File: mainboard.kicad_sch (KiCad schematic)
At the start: 90 parts, among them J1 Conn 02x05 1.27mm, J10 Conn -Z 02x05 2.00 mm, J11 Conn +X 02x05 2.00 mm, J12 Conn -X 02x05 2.00 mm, J2 USB_C_Receptacle_USB2.0, J3 Conn 02x10 1.27mm, J4 Conn +Z 02x05 2.00 mm, J5 Conn -Z 02x05 2.00 mm, J6 Conn +X 02x05 2.00 mm, J7 Conn -X 02x05 2.00 mm, J8 U.FL-R-SMT-1, J9 Conn +Z 02x05 2.00 mm, Q1 DMG2301L, SW1 KMR231NG, U1 ATSAMD51J20A-M, U10 USBLC6-2SC6, U2 MAX706RESA+, U3 AP2112K-3.3, U4 MR25H40, U5 BMX160, U6 RFM98PW, U7 DRV8830DRC, U8 DRV8830DRC, U9 DRV8830DRC, Y1 32.768kHz

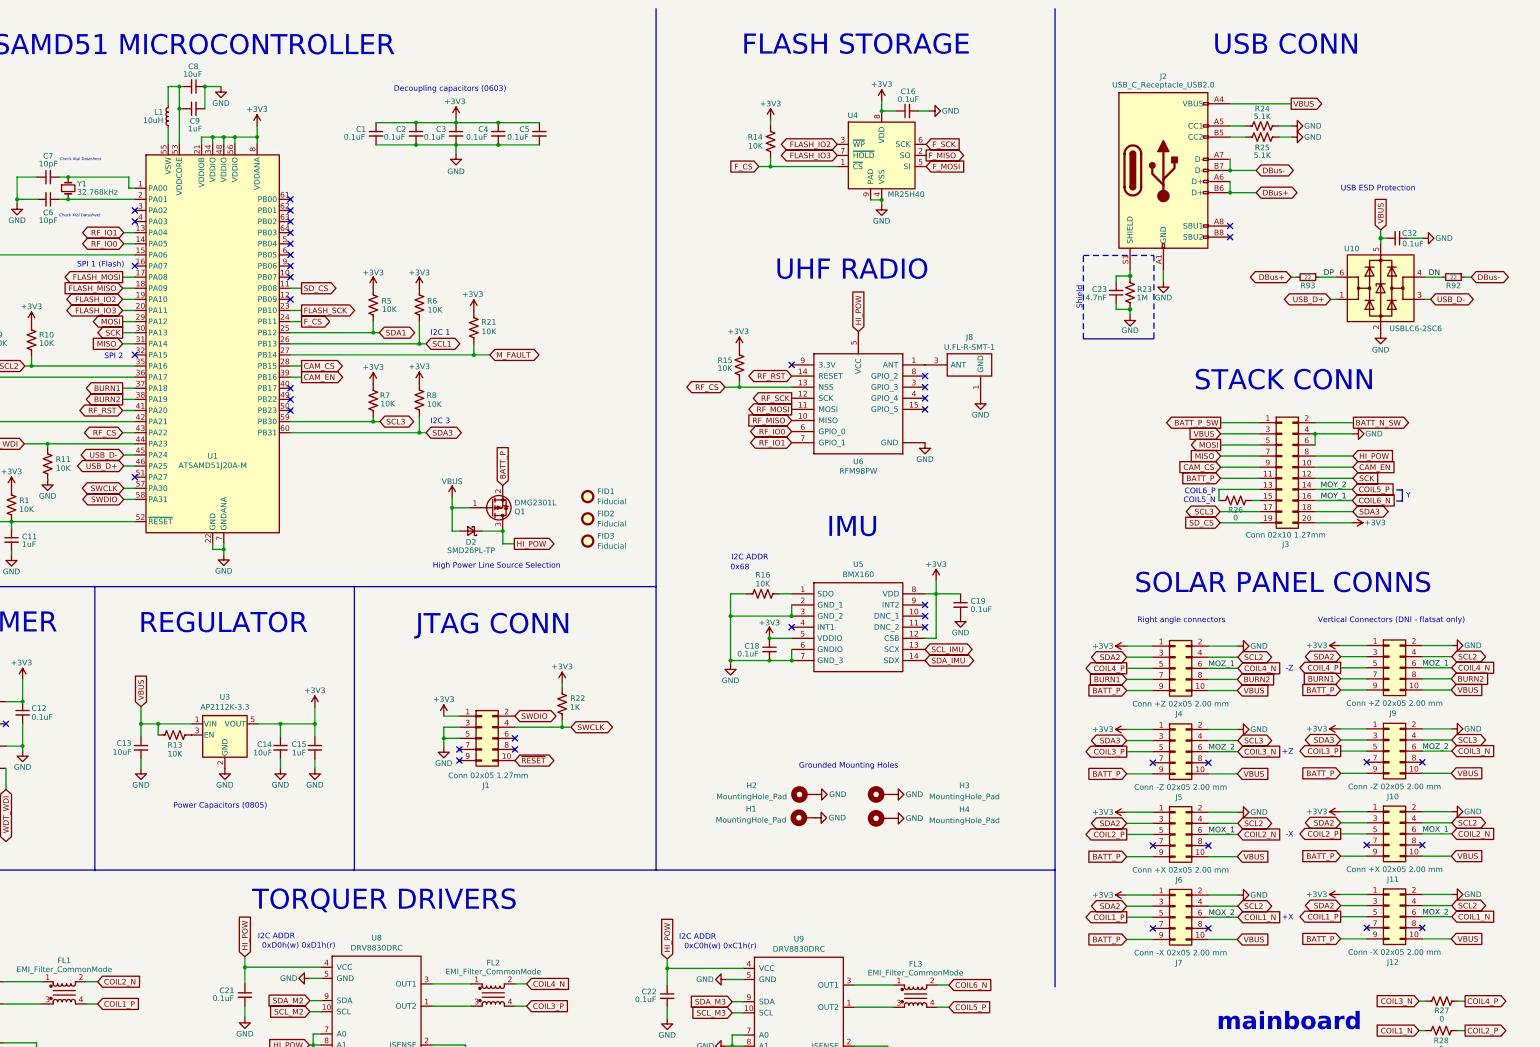
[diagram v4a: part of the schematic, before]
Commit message: Updated stack connectors and added SPDT switch
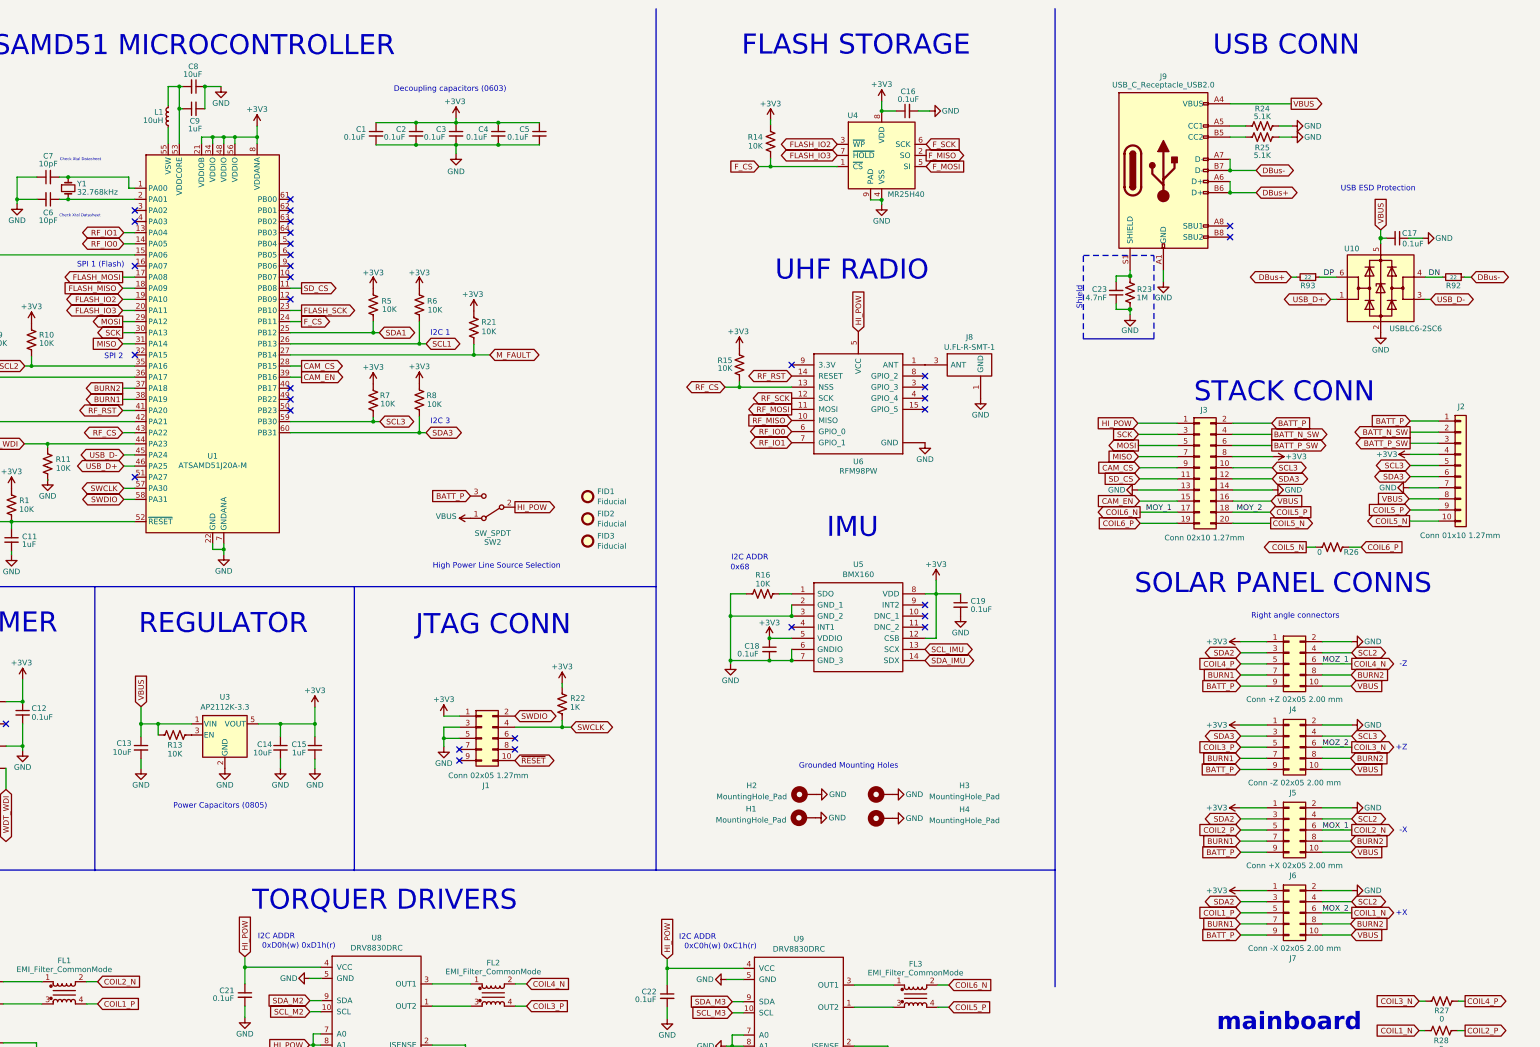
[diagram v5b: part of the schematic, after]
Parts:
- removed D2: SMD26PL-TP, Diode_SMD:D_SOD-123F, symbol Device:D_Schottky_Small
- removed J10: Conn -Z 02x05 2.00 mm, Connector_PinSocket_1.27mm:PinSocket_2x05_P1.27mm_Vertical_SMD, symbol Connector_Generic:Conn_02x05_Odd_Even
- removed J11: Conn +X 02x05 2.00 mm, Connector_PinSocket_1.27mm:PinSocket_2x05_P1.27mm_Vertical_SMD, symbol Connector_Generic:Conn_02x05_Odd_Even
- removed J12: Conn -X 02x05 2.00 mm, Connector_PinSocket_1.27mm:PinSocket_2x05_P1.27mm_Vertical_SMD, symbol Connector_Generic:Conn_02x05_Odd_Even
- removed J9: Conn +Z 02x05 2.00 mm, Connector_PinSocket_1.27mm:PinSocket_2x05_P1.27mm_Vertical_SMD, symbol Connector_Generic:Conn_02x05_Odd_Even
- removed Q1: DMG2301L, Package_TO_SOT_SMD:SOT-23, symbol Transistor_FET:DMG2301L
- added J2: Conn 01x10 1.27mm, Connector_PinSocket_1.27mm:PinSocket_1x10_P1.27mm_Vertical, symbol Connector_Generic:Conn_01x10
- added SW2: SW_SPDT, mainboard:SW_PCM12SMTR, symbol Switch:SW_SPDT
- J3: footprint Connector_PinHeader_1.27mm:PinHeader_2x10_P1.27mm_Vertical -> Connector_PinSocket_1.27mm:PinSocket_2x10_P1.27mm_Vertical
- renumbered C32 to C17, J2 to J9
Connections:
- net +3V3: now also J3.8 (Pin_8), J2.4 (Pin_4); no longer J3.20 (Pin_20)
- net BATT_N_SW: now also J3.4 (Pin_4), J2.2 (Pin_2); no longer J3.2 (Pin_2)
- net BATT_P: now also J3.2 (Pin_2), J2.1 (Pin_1), SW2.3 (C); no longer J3.11 (Pin_11)
- net BATT_P_SW: now also J3.6 (Pin_6), J2.3 (Pin_3); no longer J3.1 (Pin_1)
- net BURN1: now also J5.7 (Pin_7), J6.7 (Pin_7), J7.7 (Pin_7), U1.38 (PA19); no longer U1.37 (PA18)
- net BURN2: now also J5.8 (Pin_8), J6.8 (Pin_8), J7.8 (Pin_8), U1.37 (PA18); no longer U1.38 (PA19)
- net CAM_EN: now also J3.15 (Pin_15); no longer J3.10 (Pin_10)
- net COIL5_P: now also J3.18 (Pin_18), J2.9 (Pin_9); no longer J3.14 (Pin_14)
- net COIL6_N: now also J3.17 (Pin_17); no longer J3.16 (Pin_16)
- net GND: now also J3.13 (Pin_13), J3.14 (Pin_14), J2.7 (Pin_7); no longer J3.4 (Pin_4), J3.6 (Pin_6)
- net HI_POW: now also J3.1 (Pin_1), SW2.2 (B); no longer J3.8 (Pin_8)
- net SCK: now also J3.3 (Pin_3); no longer J3.12 (Pin_12)
- net SCL3: now also J3.10 (Pin_10), J2.5 (Pin_5); no longer J3.17 (Pin_17)
- net SDA3: now also J3.12 (Pin_12), J2.6 (Pin_6); no longer J3.18 (Pin_18)
- net SD_CS: now also J3.11 (Pin_11); no longer J3.19 (Pin_19)
- net VBUS: now also J3.16 (Pin_16), J2.8 (Pin_8), SW2.1 (A); no longer J3.3 (Pin_3)
- net COIL6_P: now reaches R26.1
- net COIL6_P: now also J3.19 (Pin_19); no longer J3.13 (Pin_13)
- net COIL5_N: now reaches R26.2
- net COIL5_N: now also J3.20 (Pin_20), J2.10 (Pin_10); no longer J3.15 (Pin_15)
- no-connect marks 47 -> 35
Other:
- note removed: "COIL5_N"
- note removed: "COIL6_P"
- note removed: "Vertical Connectors (DNI - flatsat only)"
- note removed: "Y"
- moved on the sheet: J3, J4, J5, J6, J7, R26
